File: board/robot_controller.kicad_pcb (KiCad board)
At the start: 2 copper layers, 282 parts, among them J104 JTAG-ARM, J111 UEXT, J112 UEXT, J2301 CONN_STEPPER, J2401 CONN_STEPPER, J2501 CONN_STEPPER, J2601 CONN_STEPPER, P102 CONN_1, P103 CONN_1, P104 CONN_1, P105 CONN_1, P106 CONN_1, P107 CONN_1, P108 CONN_1, P109 CONN_1, P110 CONN_1, P111 CONN_1, P112 CONN_1, P113 CONN_1, P114 CONN_1, P115 CONN_1, P116 CONN_1, P117 CONN_1, P118 CONN_1, P119 CONN_1, P120 CONN_1, P121 CONN_1, P122 CONN_1, P123 CONN_1, P124 CONN_1, P125 CONN_1, P126 CONN_1, P127 CONN_1, P128 CONN_1, P129 CONN_1, P130 CONN_1, Q401 MMBT5962, Q402 MMBT5962, Q501 MMBT5962, Q502 MMBT5962, U101 STM32F405-144, U102 FT232RL, U201 MAX6675, U2301 L6470, U2401 L6470, U2501 L6470, U2601 L6470, U301 MAX6675, X101 8MHZ

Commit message: Worked a little on the PCB layout.
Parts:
- C2307, C2308, C2309, C2310: moved to B.Cu
- moved C2302 58.0 mm to (252.1, 130.8), turned to 90 degrees
- moved C2304 56.6 mm to (249.6, 130.8), turned to 270 degrees
- moved C2309 53.0 mm to (247.0, 120.7)
- moved C2314 52.5 mm to (243.8, 130.8), turned to 270 degrees
- moved C2307 52.0 mm to (246.4, 104.1)
- moved C2303 44.8 mm to (247.7, 130.8), turned to 270 degrees
- moved R2305 44.0 mm to (262.3, 98.4), turned to 180 degrees
- moved D2301 42.7 mm to (254.6, 132.7), turned to 180 degrees
- moved C2315 34.1 mm to (245.7, 130.8), turned to 270 degrees
- moved C2310 31.9 mm to (252.1, 120.7), turned to 180 degrees
- moved C2301 29.2 mm to (254.6, 129.5)
- moved R2301 21.2 mm to (285.8, 129.5), turned to 90 degrees
- moved C2311 13.3 mm to (271.1, 115.5)
- moved P105 2.64 mm to (39.4, 47.6)
- moved C2312 2.44 mm to (290.8, 128.3)
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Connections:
- net GNDPWR renamed PGND
- C2302 pad 1: Net-(C2301-Pad1) -> Net-(C2302-Pad1)
- C2402 pad 1: Net-(C2401-Pad1) -> Net-(C2402-Pad1)
- C2502 pad 1: Net-(C2501-Pad1) -> Net-(C2502-Pad1)
- C2602 pad 1: Net-(C2601-Pad1) -> Net-(C2602-Pad1)
- D2301 pad 2: Net-(C2302-Pad2) -> Net-(C2302-Pad1)
- D2401 pad 2: Net-(C2402-Pad2) -> Net-(C2402-Pad1)
- D2501 pad 2: Net-(C2502-Pad2) -> Net-(C2502-Pad1)
- D2601 pad 2: Net-(C2602-Pad2) -> Net-(C2602-Pad1)
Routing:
- net Net-(J2301-Pad3): track 0.00 -> 46.9 mm
- net +24V: track 0.00 -> 45.9 mm
- net Net-(J2301-Pad4): track 0.00 -> 41.4 mm
- net Net-(J2301-Pad1): track 38.4 -> 0.65 mm
- net Net-(J2301-Pad2): track 17.6 -> 49.1 mm
- net Net-(C2301-Pad1): track 0.00 -> 9.01 mm
- net /Stepper 0/VREG: track 0.00 -> 8.43 mm
- net Net-(C2302-Pad2): track 0.00 -> 7.05 mm
- net /Stepper 0/OSCIN: track 0.00 -> 3.69 mm, vias 0 -> 1
- net Net-(C2302-Pad1): track 0.00 -> 3.47 mm
- net /Stepper 0/ADCIN: track 0.00 -> 3.08 mm
- net Net-(C2315-Pad1): track 0.00 -> 2.46 mm
- net /Stepper 1/OSCIN: track 0.00 -> 2.15 mm, vias 0 -> 1
- net /Stepper 0/~STBY/RST: track 0.00 -> 1.84 mm
- net (no net): vias 0 -> 3

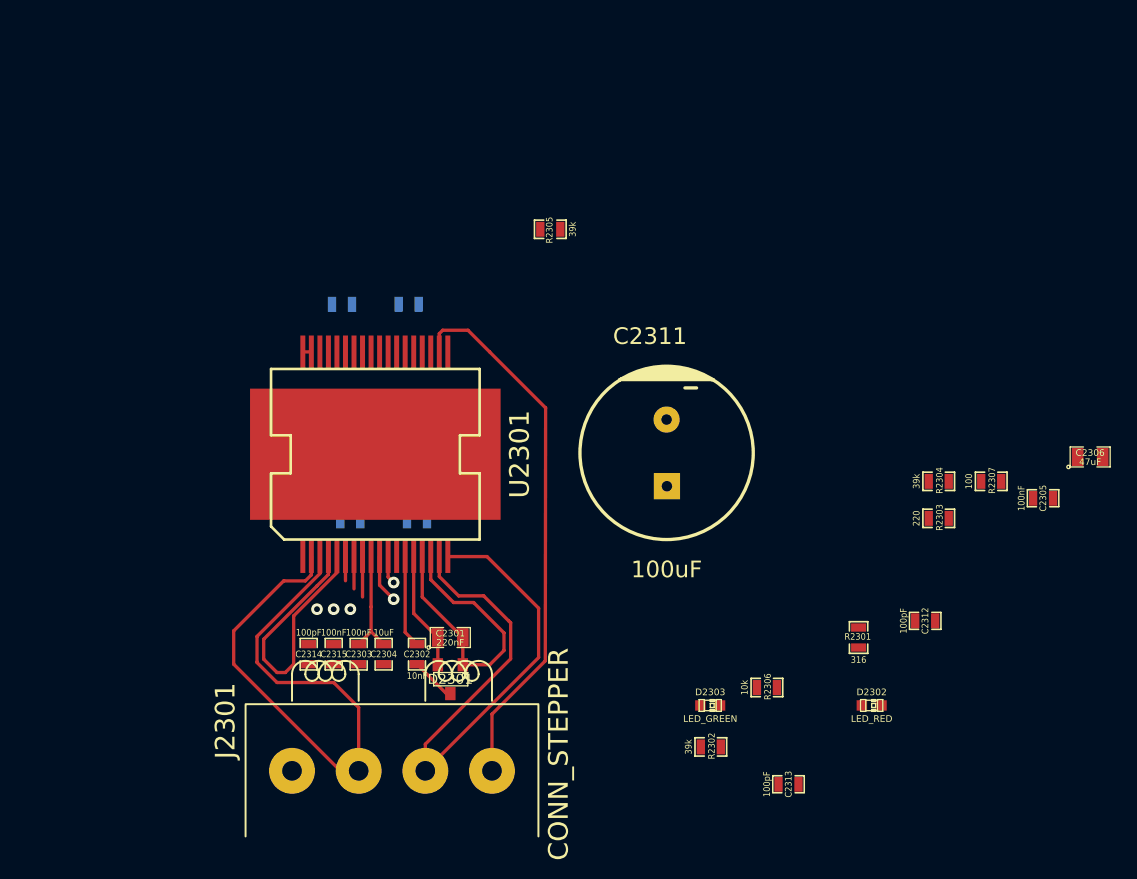
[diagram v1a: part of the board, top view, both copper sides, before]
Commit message: Worked on the stepper layout
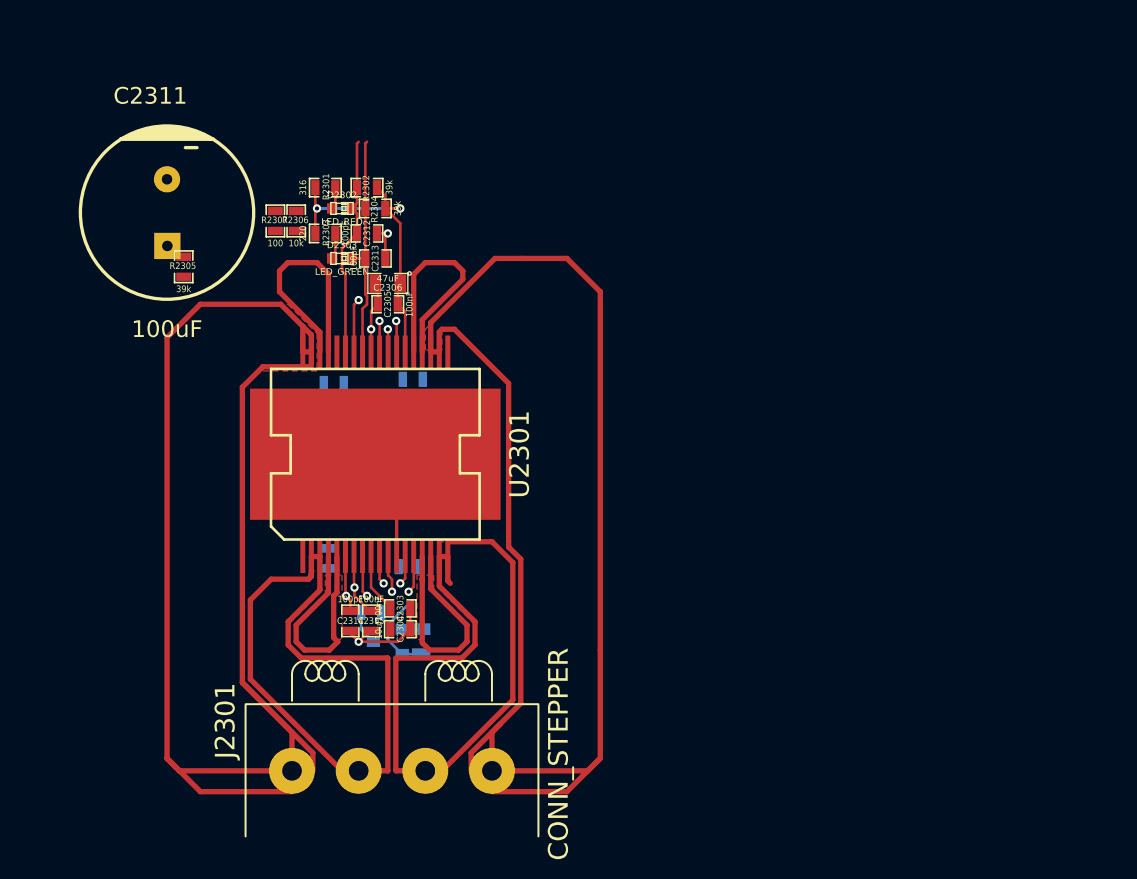
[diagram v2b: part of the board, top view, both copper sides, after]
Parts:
- C2301, C2302, D2301: moved to B.Cu
- moved R2307 58.1 mm to (241.3, 97.8), turned to 90 degrees
- moved D2302 55.4 mm to (246.4, 96.8)
- moved C2306 55.1 mm to (249.9, 102.6), turned to 180 degrees
- moved R2301 53.2 mm to (245.1, 95.2), turned to 0 degrees
- moved C2305 52.1 mm to (249.9, 104.1), turned to 180 degrees
- moved C2312 51.8 mm to (248.3, 98.7)
- moved R2303 51.5 mm to (245.1, 98.7)
- moved C2313 51.0 mm to (248.9, 100.6)
- moved R2306 50.5 mm to (242.9, 97.8), turned to 90 degrees
- moved R2302 50.0 mm to (248.3, 95.2), turned to 180 degrees
- moved R2304 47.7 mm to (248.9, 96.8), turned to 180 degrees
- moved D2303 44.1 mm to (246.4, 100.6)
- moved C2311 42.2 mm to (233.0, 97.2)
- moved R2305 28.1 mm to (234.3, 101.3), turned to 90 degrees
- moved C2307 6.07 mm to (245.7, 110.2)
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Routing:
- net Net-(J2301-Pad1): track 0.65 -> 115.9 mm
- net Net-(J2301-Pad4): track 41.4 -> 116.3 mm
- net +24V: track 45.9 -> 73.0 mm
- net +3.3V: track 0.00 -> 24.7 mm, vias 0 -> 2
- net /Stepper 0/~BUSY~/SYNC: track 0.00 -> 17.3 mm
- net /Stepper 0/~FLAG: track 0.00 -> 17.0 mm
- net GND: track 0.00 -> 16.6 mm, vias 0 -> 3
- net PGND: track 0.00 -> 6.18 mm
- net Net-(J2301-Pad3): track 46.9 -> 52.7 mm
- net Net-(C2302-Pad2): track 7.05 -> 2.39 mm, vias 0 -> 1
- net /Stepper 0/~CS: track 0.00 -> 4.09 mm, vias 0 -> 1
- net /Stepper 0/VREG: track 8.43 -> 4.56 mm
- net Net-(C2315-Pad1): track 2.46 -> 4.94 mm, vias 0 -> 1
- net /Stepper 0/~STBY/RST: track 1.84 -> 4.29 mm, vias 0 -> 1
- net /Stepper 0/SDO: track 0.00 -> 2.38 mm, vias 0 -> 1
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- added copper zone on F.Cu, net +24V
- added copper zone on F.Cu, net Net-(J2301-Pad1)
- added copper zone on F.Cu, net Net-(J2301-Pad2)
- added copper zone on F.Cu, net Net-(J2301-Pad3)
- added copper zone on F.Cu, net Net-(J2301-Pad4)
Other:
- net class Default: clearance 0.254 -> 0.2032; trace_width 0.254 -> 0.2032; via_dia 0.889 -> 0.635; via_drill 0.635 -> 0.4318
- net class Power added: clearance 0.3048, trace_width 1.2192, via_dia 0.635, via_drill 0.4318
- rule pad_to_mask_clearance: 0.2 -> 0.2032
- rule trace_clearance: 0.254 -> 0.2032
- rule trace_min: 0.254 -> 0.2032
- rule via_min_drill: 0.508 -> 0.4064
- rule via_min_size: 0.889 -> 0.635

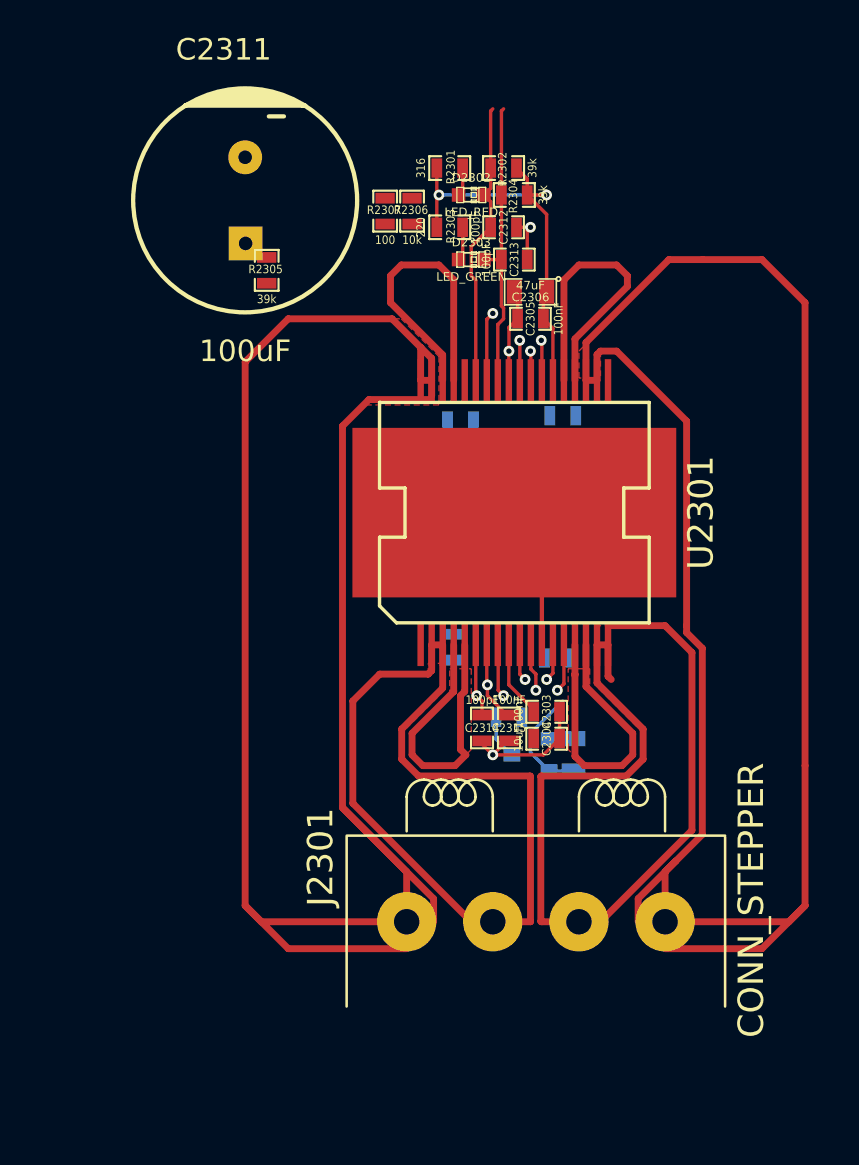
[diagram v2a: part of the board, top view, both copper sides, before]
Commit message: Added vias of proper sizes for 24V near the stepper drivers
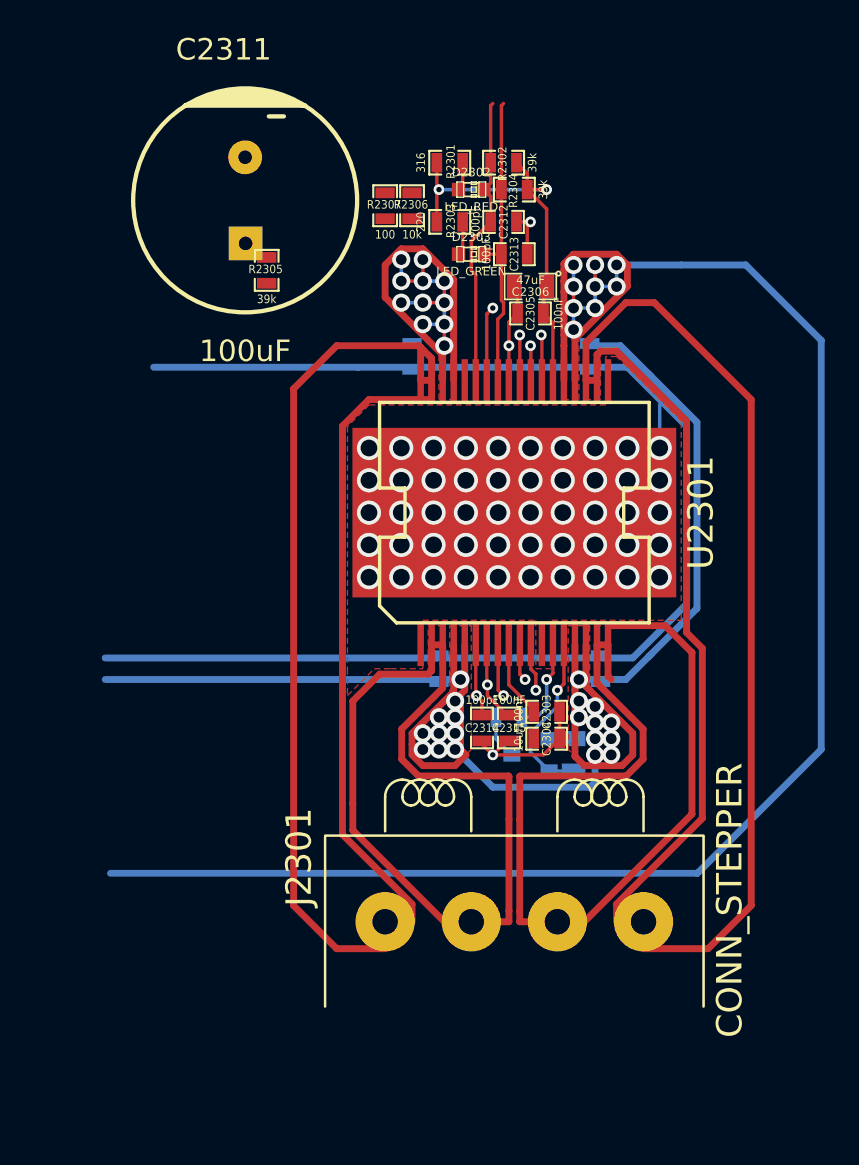
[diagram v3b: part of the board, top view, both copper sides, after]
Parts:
- moved C2307 4.76 mm to (242.9, 106.4), turned to 270 degrees
- moved C2308 3.84 mm to (253.4, 106.4), turned to 270 degrees
- moved C2310 2.62 mm to (254.0, 124.8), turned to 90 degrees
- moved C2309 1.59 mm to (244.5, 124.8)
- moved J2301 1.27 mm to (248.9, 139.7)
- moved C2312 0.32 mm to (248.3, 98.4)
- moved D2302 0.32 mm to (246.4, 96.5)
- moved R2303 0.32 mm to (245.1, 98.4)
- moved R2304 0.32 mm to (248.9, 96.5)
- moved R2306 0.32 mm to (242.9, 97.5)
- moved R2307 0.32 mm to (241.3, 97.5)
- moved C2305 0.32 mm to (249.9, 103.8)
- moved C2306 0.32 mm to (249.9, 102.2)
- moved C2313 0.32 mm to (248.9, 100.3)
- moved D2303 0.32 mm to (246.4, 100.3)
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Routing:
- net +24V: track 73.0 -> 260.9 mm, vias 0 -> 40
- net PGND: track 6.18 -> 175.9 mm, vias 0 -> 50
- net Net-(J2301-Pad1): track 115.9 -> 87.9 mm
- net Net-(J2301-Pad4): track 116.3 -> 93.8 mm
- net Net-(C2302-Pad2): track 2.39 -> 5.73 mm
- net Net-(J2301-Pad2): track 48.8 -> 46.5 mm
- net Net-(J2301-Pad3): track 52.7 -> 51.5 mm
- net Net-(C2301-Pad1): track 9.65 -> 10.2 mm
- added copper zone on F.Cu, net PGND

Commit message: Worked on a way to route the 5 wires underneath the capacitor.
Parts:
- C109, C2307, C2308, C2309, C2310, C2407, C2408, C2409, C2410, C2507, C2508, C2509, C2510, C2607, C2608, C2609, C2610: footprint SMD_Packages:SM0603_Capa -> Capacitors_SMD:c_1808
- moved C2307 2.56 mm to (240.3, 106.0), turned to 90 degrees
- moved C2308 2.25 mm to (255.6, 106.0), turned to 90 degrees
- moved C2310 1.77 mm to (255.6, 124.0), turned to 270 degrees
- moved C2309 1.50 mm to (243.2, 124.0), turned to 270 degrees
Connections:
- C108 pad 2: PGND -> GND
- C109 pad 2: PGND -> GND
- C2307 pad 2: PGND -> GND
- C2308 pad 2: PGND -> GND
- C2309 pad 2: PGND -> GND
- C2310 pad 2: PGND -> GND
- C2311 pad 2: PGND -> GND
- C2407 pad 2: PGND -> GND
- C2408 pad 2: PGND -> GND
- C2409 pad 2: PGND -> GND
- C2410 pad 2: PGND -> GND
- C2411 pad 2: PGND -> GND
- C2507 pad 2: PGND -> GND
- C2508 pad 2: PGND -> GND
- C2509 pad 2: PGND -> GND
- C2510 pad 2: PGND -> GND
- C2511 pad 2: PGND -> GND
- C2607 pad 2: PGND -> GND
- C2608 pad 2: PGND -> GND
- C2609 pad 2: PGND -> GND
- C2610 pad 2: PGND -> GND
- C2611 pad 2: PGND -> GND
- C604 pad 1: (no net) -> Net-(C604-Pad1)
- D1501 pad 1: (no net) -> /Industrial Output 0/Sink
- D1601 pad 1: (no net) -> /Industrial Output 1/Sink
- D1701 pad 1: (no net) -> /Industrial Output 2/Sink
- D1801 pad 1: (no net) -> /Industrial Output 3/Sink
- D1901 pad 1: (no net) -> /Industrial Output 4/Sink
- D2001 pad 1: (no net) -> /Industrial Output 5/Sink
- D2101 pad 1: (no net) -> /Industrial Output 6/Sink
- D2201 pad 1: (no net) -> /Industrial Output 7/Sink
- J111 pad 1: (no net) -> Net-(J111-Pad1)
- J112 pad 1: (no net) -> Net-(J112-Pad1)
- R1001 pad 1: (no net) -> /Industrial Input 3/A/D_Input
- R103 pad 2: (no net) -> Net-(Q101-Pad2)
- R106 pad 2: (no net) -> Net-(Q101-Pad3)
- R1101 pad 1: (no net) -> /Industrial Input 4/A/D_Input
- R1201 pad 1: (no net) -> /Industrial Input 5/A/D_Input
- R1301 pad 1: (no net) -> /Industrial Input 6/A/D_Input
- R1401 pad 1: (no net) -> /Industrial Input 7/A/D_Input
- R1501 pad 2: (no net) -> Net-(Q1501-Pad2)
- R1601 pad 2: (no net) -> Net-(Q1601-Pad2)
- R1701 pad 2: (no net) -> Net-(Q1701-Pad2)
- R1801 pad 2: (no net) -> Net-(Q1801-Pad2)
- R1901 pad 2: (no net) -> Net-(Q1901-Pad2)
- R2001 pad 2: (no net) -> Net-(Q2001-Pad2)
- R2101 pad 2: (no net) -> Net-(Q2101-Pad2)
- R2201 pad 2: (no net) -> Net-(Q2201-Pad2)
- R2307 pad 1: (no net) -> Net-(J2302-Pad2)
- R2407 pad 1: (no net) -> Net-(J2402-Pad2)
- R2507 pad 1: (no net) -> Net-(J2502-Pad2)
- R2607 pad 1: (no net) -> Net-(J2602-Pad2)
- R602 pad 2: (no net) -> Net-(R602-Pad2)
- R701 pad 1: (no net) -> /Industrial Input 0/A/D_Input
- R801 pad 1: (no net) -> /Industrial Input 1/A/D_Input
- R901 pad 1: (no net) -> /Industrial Input 2/A/D_Input
- U101 pad 1: (no net) -> Net-(U101-Pad1)
- U101 pad 113: (no net) -> Net-(U101-Pad113)
- U101 pad 118: (no net) -> Net-(U101-Pad118)
- U101 pad 12: (no net) -> Net-(U101-Pad12)
- U101 pad 123: (no net) -> Net-(U101-Pad123)
- U101 pad 135: (no net) -> Net-(U101-Pad135)
- U101 pad 136: (no net) -> Net-(U101-Pad136)
- U101 pad 137: (no net) -> Net-(U101-Pad137)
- U101 pad 141: (no net) -> Net-(U101-Pad141)
- U101 pad 142: (no net) -> Net-(U101-Pad142)
- U101 pad 2: (no net) -> Net-(U101-Pad2)
- U101 pad 3: (no net) -> Net-(U101-Pad3)
- U101 pad 47: (no net) -> Net-(U101-Pad47)
- U101 pad 49: (no net) -> Net-(U101-Pad49)
- U101 pad 5: (no net) -> Net-(U101-Pad5)
- U101 pad 58: (no net) -> Net-(U101-Pad58)
- U101 pad 59: (no net) -> Net-(U101-Pad59)
- U101 pad 63: (no net) -> Net-(U101-Pad63)
- U101 pad 70: (no net) -> Net-(U101-Pad70)
- U101 pad 73: (no net) -> Net-(U101-Pad73)
- U101 pad 74: (no net) -> /USB_VBUS
- U101 pad 75: (no net) -> /USB_DM
- U101 pad 76: (no net) -> /USB_DP
- U101 pad 79: (no net) -> Net-(U101-Pad79)
- U101 pad 8: (no net) -> Net-(U101-Pad8)
- U101 pad 80: (no net) -> Net-(U101-Pad80)
- U101 pad 87: (no net) -> Net-(U101-Pad87)
- U101 pad 9: (no net) -> Net-(U101-Pad9)
- U101 pad 96: (no net) -> /USART6_TX
- U101 pad 97: (no net) -> /USART6_RX
- U102 pad 10: (no net) -> Net-(U102-Pad10)
- U102 pad 12: (no net) -> Net-(U102-Pad12)
- U102 pad 13: (no net) -> Net-(U102-Pad13)
- U102 pad 15: (no net) -> Net-(J106-Pad3)
- U102 pad 16: (no net) -> Net-(J106-Pad2)
- U102 pad 19: (no net) -> Net-(U102-Pad19)
- U102 pad 2: (no net) -> Net-(U102-Pad2)
- U102 pad 27: (no net) -> Net-(U102-Pad27)
- U102 pad 28: (no net) -> Net-(U102-Pad28)
- U102 pad 6: (no net) -> Net-(U102-Pad6)
- U102 pad 9: (no net) -> Net-(U102-Pad9)
- U201 pad 3: (no net) -> Net-(J201-Pad2)
- U2301 pad 1: PGND -> GND
- U2301 pad 12: PGND -> GND
- U2301 pad 19: PGND -> GND
- U2301 pad PAD: PGND -> GND
- U2401 pad 1: PGND -> GND
- U2401 pad 11: (no net) -> /Stepper 1/OSCOUT
- U2401 pad 12: PGND -> GND
- U2401 pad 19: PGND -> GND
- U2401 pad PAD: PGND -> GND
- U2501 pad 1: PGND -> GND
- U2501 pad 11: (no net) -> /Stepper 2/OSCOUT
- U2501 pad 12: PGND -> GND
- U2501 pad 19: PGND -> GND
- U2501 pad PAD: PGND -> GND
- U2601 pad 1: PGND -> GND
- U2601 pad 11: (no net) -> /Stepper 3/OSCOUT
- U2601 pad 12: PGND -> GND
- U2601 pad 19: PGND -> GND
- U2601 pad PAD: PGND -> GND
- U301 pad 3: (no net) -> Net-(J301-Pad2)
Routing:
- net PGND: track 175.9 -> 0.00 mm, vias 50 -> 0
- net GND: track 16.6 -> 125.7 mm, vias 3 -> 53
- net +24V: track 260.9 -> 211.3 mm
- net /Stepper 0/~STBY/RST: track 4.29 -> 38.4 mm
- net /Stepper 0/ADCIN: track 3.17 -> 15.0 mm
- net Net-(C2315-Pad1): track 4.94 -> 16.7 mm
- net /Stepper 0/OSCIN: track 2.17 -> 12.0 mm
- net /Stepper 1/OSCIN: track 2.80 -> 12.5 mm
- net /Stepper 0/VREG: track 4.56 -> 6.71 mm

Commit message: Stepper Driver layout almost done, updated some of the footprints based on Andrew's work.
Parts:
- added J201: CONN_2, components:CONN_TEMP, F.Cu at (56.5, 147.6)
- added J301: CONN_2, components:CONN_TEMP, F.Cu at (34.3, 147.0)
- added Q101: PNP, components:SOT23-EXTRASPECIAL, F.Cu at (65.1, 70.8)
- added Q1501: NJT4031NT1G, components:SOT223-EXTRASPECIAL, F.Cu at (28.6, 84.1)
- added Q1601: NJT4031NT1G, components:SOT223-EXTRASPECIAL, F.Cu at (39.7, 84.5)
- added Q1701: NJT4031NT1G, components:SOT223-EXTRASPECIAL, F.Cu at (48.9, 85.7)
- added Q1801: NJT4031NT1G, components:SOT223-EXTRASPECIAL, F.Cu at (61.9, 86.4)
- added Q1901: NJT4031NT1G, components:SOT223-EXTRASPECIAL, F.Cu at (74.3, 85.4)
- added Q2001: NJT4031NT1G, components:SOT223-EXTRASPECIAL, F.Cu at (84.8, 86.0)
- added Q2101: NJT4031NT1G, components:SOT223-EXTRASPECIAL, F.Cu at (97.5, 85.7)
- added Q2201: NJT4031NT1G, components:SOT223-EXTRASPECIAL, F.Cu at (108.3, 85.4)
- added U601: LMZ14201, components:PFM7, F.Cu at (118.4, 84.1)
- D1001, D1101, D1201, D1301, D1401, D701, D801, D901: footprint SMD_Packages:SOT23-SPECIAL -> components:SOT23-EXTRASPECIAL
- moved R2307 51.0 mm to (264.5, 142.9), turned to 180 degrees
- moved R2306 48.6 mm to (264.5, 141.0), turned to 180 degrees
- moved C2311 31.2 mm to (263.8, 101.9)
- moved R2305 9.14 mm to (242.9, 98.1), turned to 270 degrees
- moved U301 2.39 mm to (34.3, 136.5)
- moved C2307 0.95 mm to (240.3, 107.0)
- moved C2308 0.95 mm to (255.6, 107.0)
- moved C2304 0.45 mm to (251.1, 129.2)
- moved C2309 0.16 mm to (243.2, 124.1)
- moved C2310 0.16 mm to (255.6, 124.1)
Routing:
- net +24V: track 211.3 -> 265.5 mm
- net /Stepper 1/OSCIN: track 12.5 -> 64.2 mm, vias 1 -> 2
- net /Stepper 0/OSCIN: track 12.0 -> 63.2 mm, vias 1 -> 2
- net /Stepper 0/ADCIN: track 15.0 -> 65.7 mm, vias 1 -> 2
- net +3.3V: track 24.7 -> 72.2 mm
- net (no net): track 0.00 -> 42.7 mm
- net /Stepper 0/~STBY/RST: track 38.4 -> 70.1 mm, vias 1 -> 2
- net GND: track 125.7 -> 152.2 mm
- net Net-(C2315-Pad1): track 16.7 -> 36.1 mm, vias 1 -> 0
- net /Stepper 0/SCK: track 1.73 -> 9.75 mm
- net /Stepper 0/SDI: track 2.36 -> 8.99 mm
- net /Stepper 0/SDO: track 2.38 -> 8.14 mm
- net /Stepper 0/~CS: track 4.09 -> 9.31 mm
- net /Stepper 0/STCK: track 0.00 -> 5.13 mm, vias 0 -> 1
- net Net-(J2301-Pad2): track 46.5 -> 47.5 mm
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- added copper zone on F.Cu, net GND
- removed copper zone on F.Cu, net PGND
